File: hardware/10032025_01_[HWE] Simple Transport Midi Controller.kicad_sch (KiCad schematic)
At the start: 0 parts

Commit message: feat![HWE]: Changed MCU to Adafruit ESP32-S3
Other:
- company: (none) -> Madueke Systems and Technologies
- title: (none) -> Simple Midi Transport Controller
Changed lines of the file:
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@@
 	(generator_version "9.0")
 	(paper "A4")
+	(title_block
+		(title "Simple Midi Transport Controller")
+		(date "2026-04-06")
+		(rev "1")
+		(company "Madueke Systems and Technologies")
+		(comment 1 "Used the combination of the Adafruit Feather ESP32-V2 Dev Board and the SX1509 IO expander")
+	)
 	(wire
 		(pts

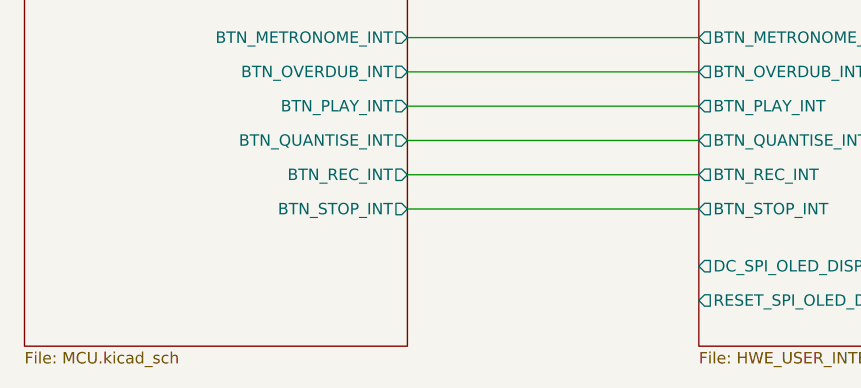
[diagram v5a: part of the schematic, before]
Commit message: feat [HWE]: Added probe points to SPI connections
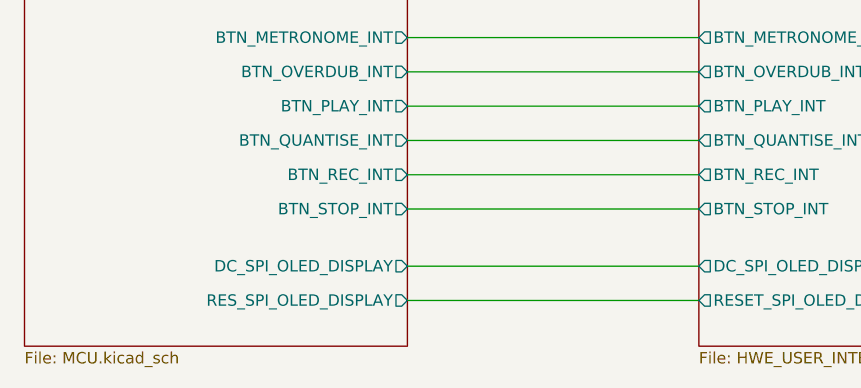
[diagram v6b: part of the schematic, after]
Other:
- sheet Microcontroller Unit ports: added DC_SPI_OLED_DISPLAY, RES_SPI_OLED_DISPLAY; removed none
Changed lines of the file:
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@@
+	(wire
+		(pts
+			(xy 131.445 130.81) (xy 163.83 130.81)
+		)
+		(stroke
+			(width 0)
+			(type default)
+		)
+	)
+	(wire
+		(pts
+			(xy 131.445 134.62) (xy 163.83 134.62)
+		)
+		(stroke
+			(width 0)
+			(type default)
+		)
+	)
 	(wire
 		(pts
@@
 			(effects
 				(font
+					(size 1.27 1.27)
+				)
+				(justify right)
+			)
+		)
+		(pin "DC_SPI_OLED_DISPLAY" output
+			(at 131.445 130.81 0)
+			(effects
+				(font
+					(size 1.27 1.27)
+				)
+				(justify right)
+			)
+		)
+		(pin "RES_SPI_OLED_DISPLAY" output
+			(at 131.445 134.62 0)
+			(effects
+				(font
